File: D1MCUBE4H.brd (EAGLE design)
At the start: 100 x 100 mm, 10 parts

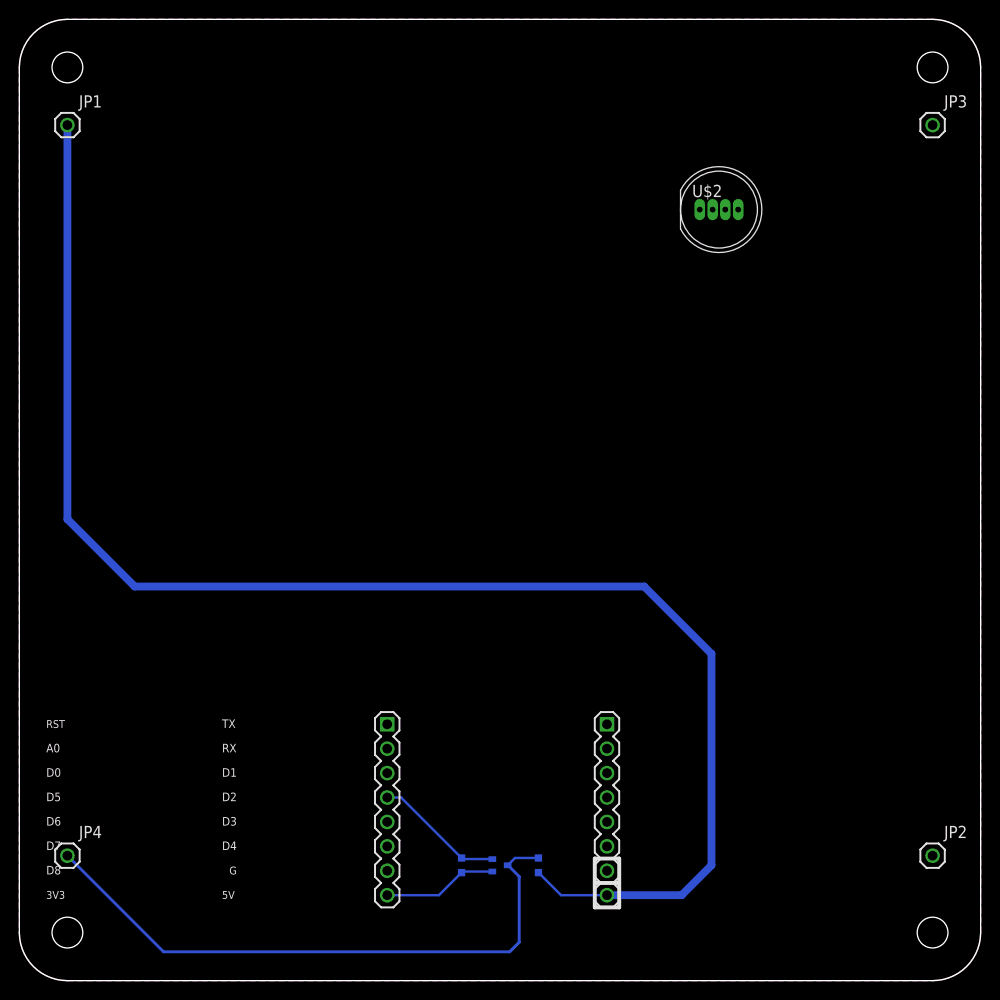
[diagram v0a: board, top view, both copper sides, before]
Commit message: Moved horizontal plane files into the same project
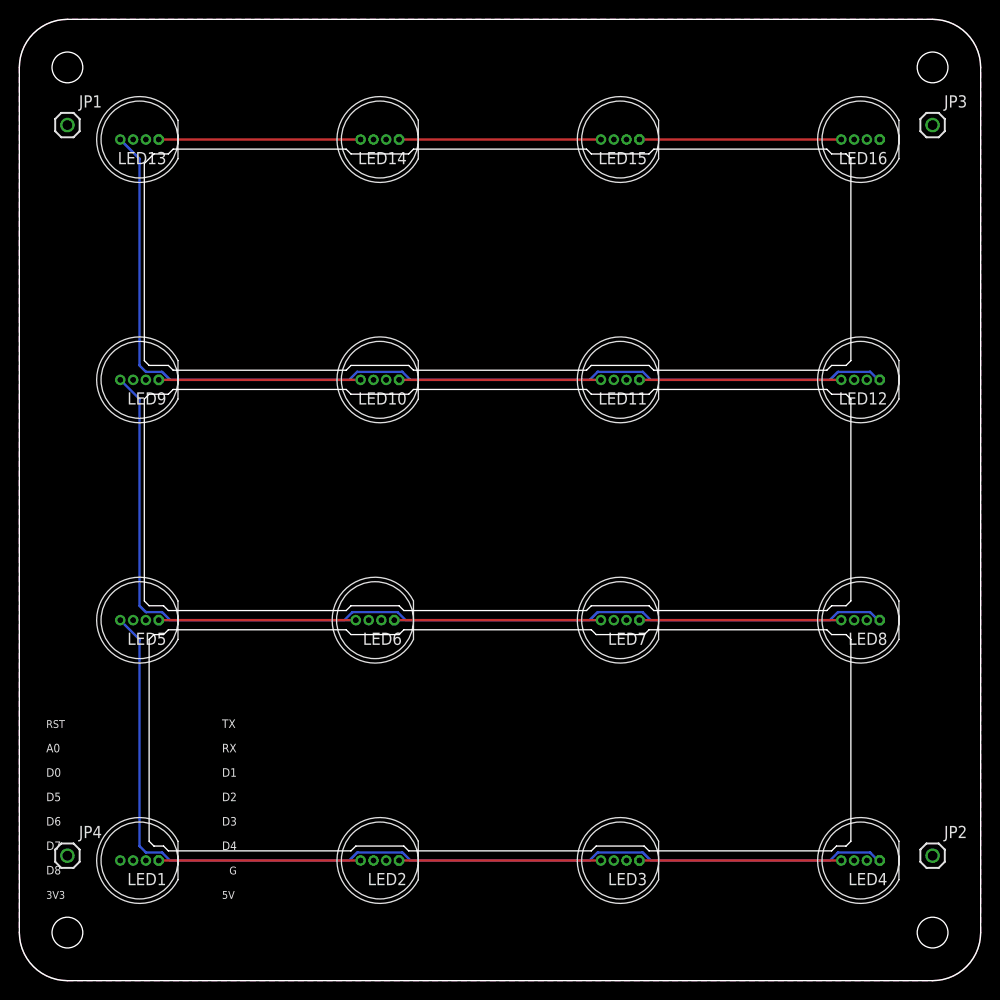
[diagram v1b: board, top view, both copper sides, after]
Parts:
- removed H1, H2: (no value), freetronics-original:1X08
- removed R1, R2: 10k, freetronics-jon:0603
- removed U$2: APA106F8, freetronics-jon:LED8MMRGB
- removed U$3: RJU003N03, freetronics-jon:SOT32-3
- added LED1, LED10, LED11, LED12, LED13, LED14, LED15, LED16, LED2, LED3, LED4, LED5, LED6, LED7, LED8, LED9: APA106F8, freetronics-jon:LED8MMRGB
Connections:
- removed net 3.3V: H1.8, R1.2, U$3.1
- removed net A0: H1.2
- removed net D0: H1.3
- removed net D1: H2.3
- removed net D2: H2.4
- removed net D3: H2.5
- removed net D4: H2.6
- removed net D5: H1.4, R1.1, U$3.2
- removed net D6: H1.5
- removed net D7: H1.6
- removed net D8: H1.7
- removed net DATA: JP4.1, R2.1, U$3.3
- removed net RST: H1.1
- removed net RX: H2.2
- removed net TX: H2.1
- removed net VDD: U$2.3
- new net DIN: JP4.1, LED1.4
- new net DOUT: LED16.1
- new net N$1: LED1.1, LED2.4
- new net N$10: LED11.1, LED12.4
- new net N$11: LED5.1, LED6.4
- new net N$12: LED6.1, LED7.4
- new net N$13: LED7.1, LED8.4
- new net N$16: LED12.1, LED13.4
- new net N$17: LED4.1, LED5.4
- new net N$18: LED8.1, LED9.4
- new net N$2: LED2.1, LED3.4
- new net N$3: LED3.1, LED4.4
- new net N$5: LED13.1, LED14.4
- new net N$6: LED14.1, LED15.4
- new net N$7: LED15.1, LED16.4
- new net N$8: LED10.4, LED9.1
- new net N$9: LED10.1, LED11.4
- net 5V: now also LED1.3, LED10.3, LED11.3, LED12.3, LED13.3, LED14.3, LED15.3, LED16.3, LED2.3, LED3.3, LED4.3, LED5.3, LED6.3, LED7.3, LED8.3, LED9.3; no longer H2.8, R2.2
- net GND: now also LED1.2, LED10.2, LED11.2, LED12.2, LED13.2, LED14.2, LED15.2, LED16.2, LED2.2, LED3.2, LED4.2, LED5.2, LED6.2, LED7.2, LED8.2, LED9.2; no longer H2.7, U$2.2
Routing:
- net 5V: track 156.1 -> 0.00 mm
- net N$18: track 0.00 -> 104.0 mm
- net N$17: track 0.00 -> 104.0 mm
- net N$16: track 0.00 -> 104.0 mm
- net DATA: track 63.6 -> 0.00 mm
- net N$12: track 0.00 -> 21.5 mm
- net N$9: track 0.00 -> 21.0 mm
- net N$8: track 0.00 -> 21.0 mm
- net N$7: track 0.00 -> 21.0 mm
- net N$6: track 0.00 -> 21.0 mm
- net N$5: track 0.00 -> 21.0 mm
- net N$3: track 0.00 -> 21.0 mm
- net N$2: track 0.00 -> 21.0 mm
- net N$13: track 0.00 -> 21.0 mm
- net N$10: track 0.00 -> 21.0 mm
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- added copper zone on layer 16, net 5V
- removed copper zone on layer 16, net GND
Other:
- outline, holes or cut-outs redrawn
